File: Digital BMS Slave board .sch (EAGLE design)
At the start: 268 parts, among them J1 S7B-PH-K, J10 S3B-PH-K, J11 S4B-PH-K, J2 S4B-PH-K, J3 S4B-PH-K, J4 S6B-PH-K, J5 S2B-PH-K, J6 S2B-PH-K, J7 S2B-PH-K, J8 S2B-PH-K, J9 S3B-PH-K, Q1 BSS123, Q2 BSS123, Q3 BSS123, Q4 BSS123, Q5 BSS123, Q6 BSS123, U1 BQ79606A-Q1-HTQFP(PHP)|48, X2 PESD2CAN, X3 PESD2CAN, X4 PESD2CAN, X5 PESD2CAN

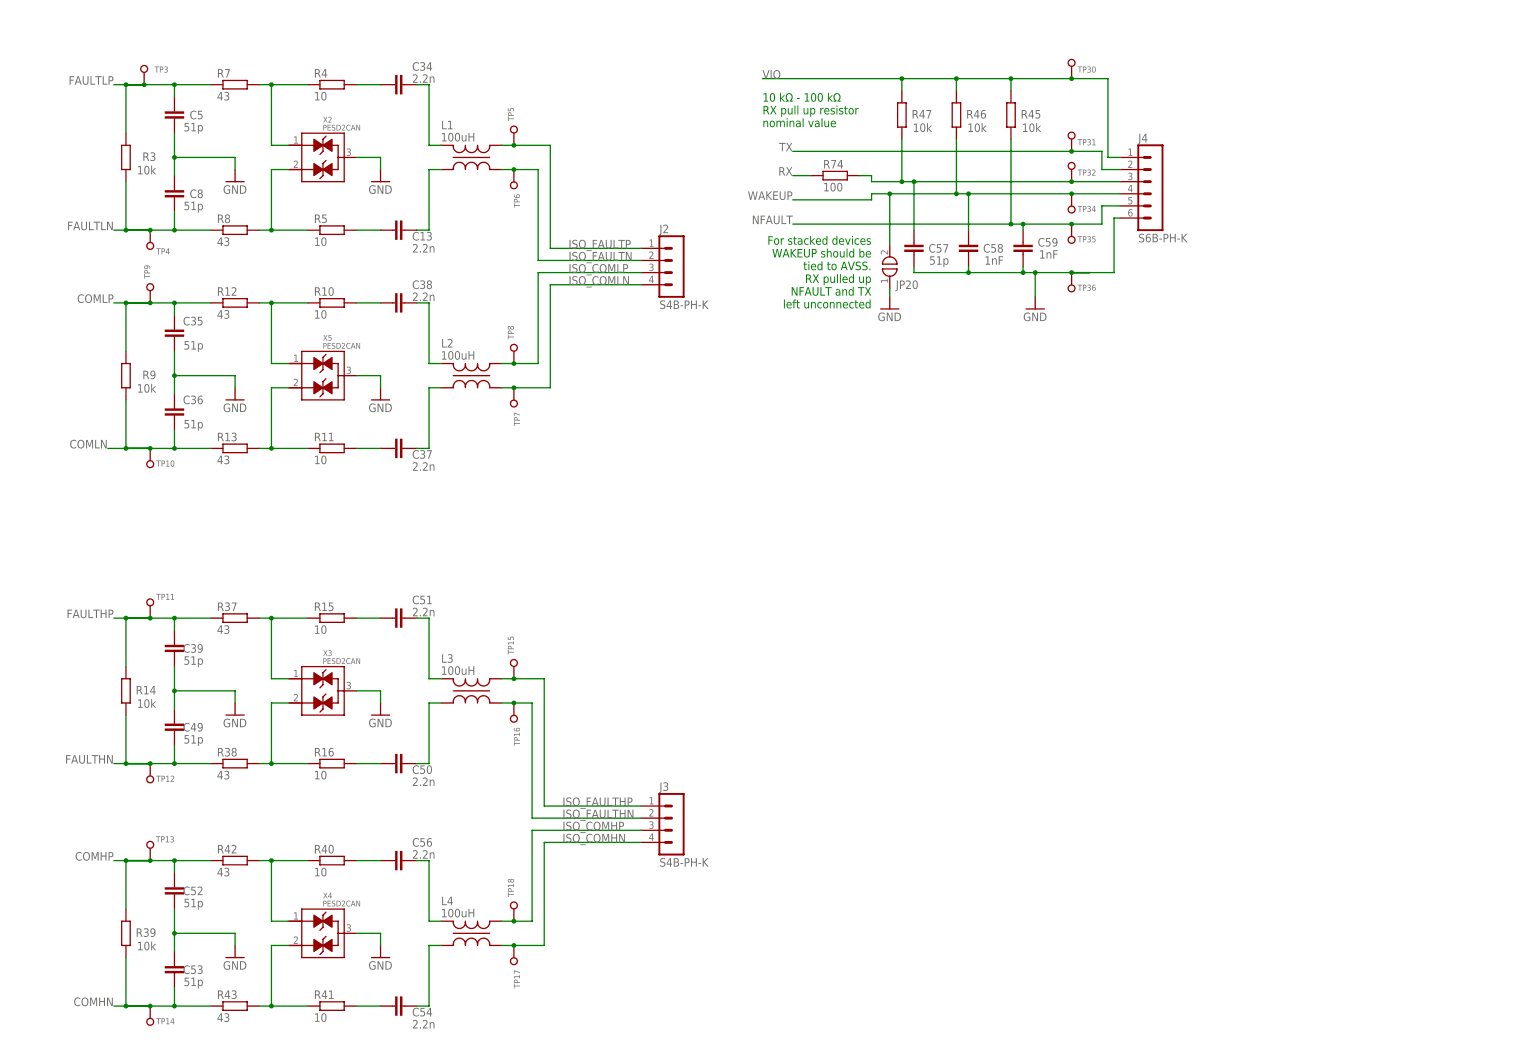
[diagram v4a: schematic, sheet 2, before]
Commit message: components placed on board
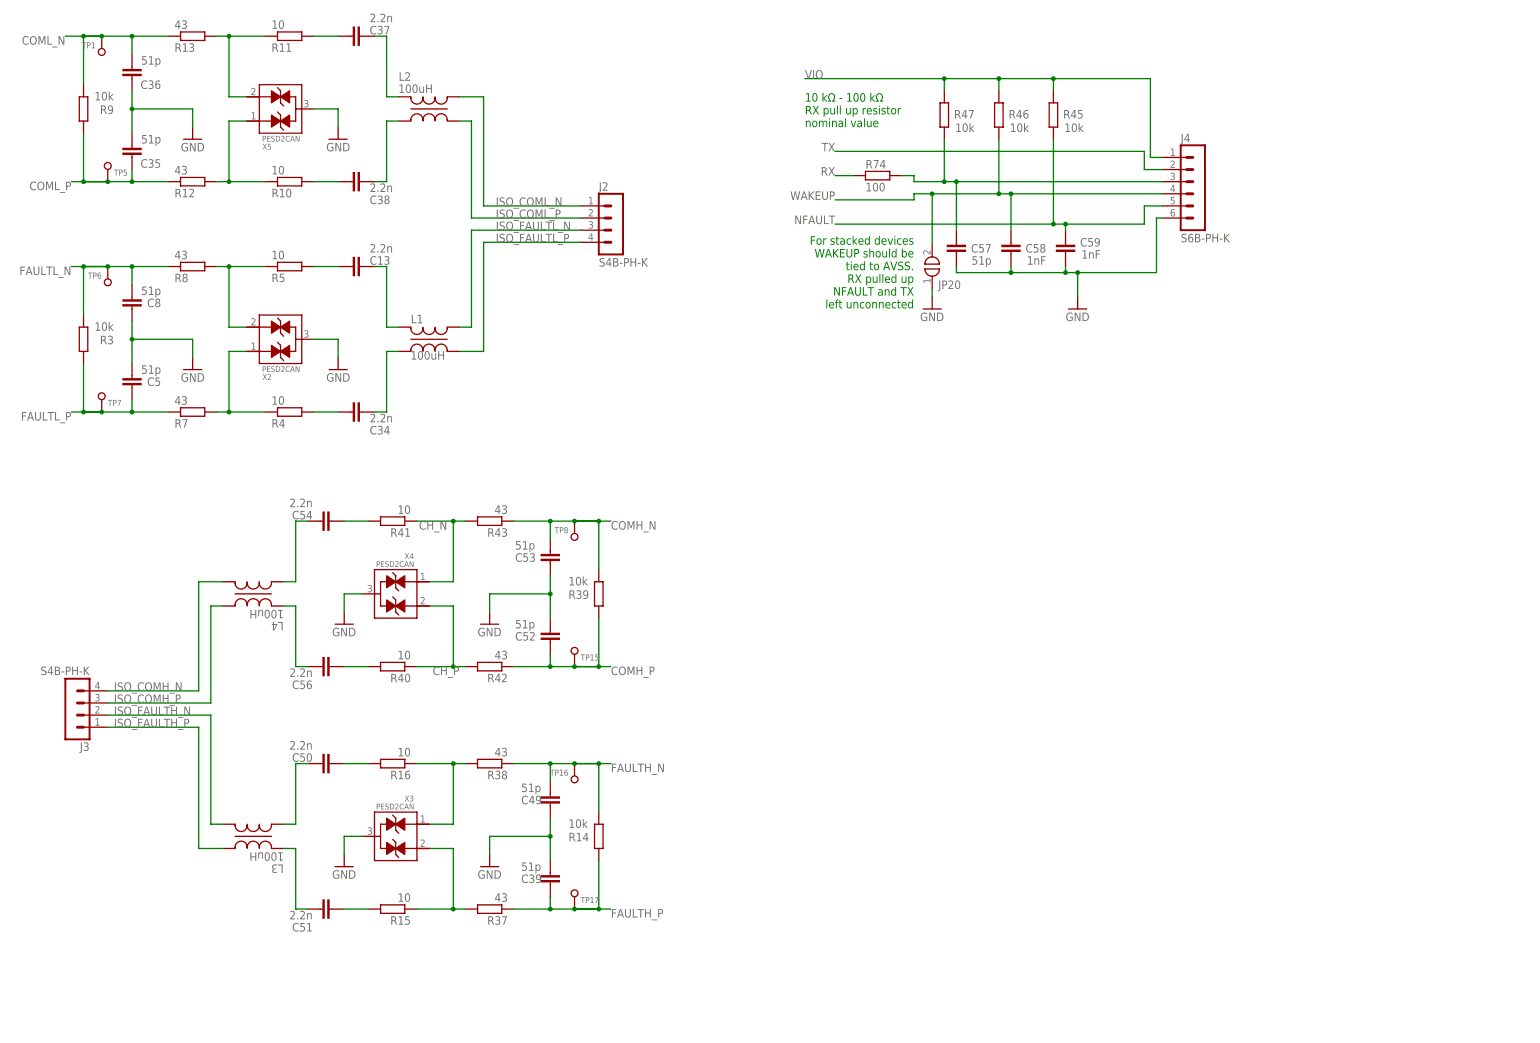
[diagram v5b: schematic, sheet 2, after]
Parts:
- removed JP4: 1x7, commonly used connectors:PINHD-1X7-OCT
- removed JP5: 2x7, pinhead:PINHD-2X7
- removed TP14, TP18, TP19, TP20, TP21, TP22, TP23, TP24, TP25, TP26, TP27, TP28, TP29, TP33: TEST_PAD2, testing:TEST_PAD2
- removed TP30, TP31, TP32, TP34, TP35, TP36, TP37, TP39, TP41, TP44, TP45, TP46, TP47, TP48, TP49, TP50: TEST_PAD, testing:TEST_PAD
- added J12: S4B-PH-K, con-jst-ph:S4B-PH-K
- J1: value S7B-PH-K -> S4B-PH-K; device con-jst-ph:S7B-PH-K -> con-jst-ph:S4B-PH-K
- TP1, TP10, TP11, TP12, TP15, TP16, TP17, TP3, TP4, TP5, TP6, TP7, TP8, TP9: value TEST_PAD2 -> TEST_PAD; device testing:TEST_PAD2 -> testing:TEST_PAD
- TP13: value TEST_PAD2 -> TEST_PAD1; device testing:TEST_PAD2 -> testing:TEST_PAD1
- U1: value BQ79606A-Q1-HTQFP(PHP)|48 -> BQ79606A-Q1-[HTQFP(PHP)|48]; device texas Instrumets:BQ79606A-Q1-HTQFP(PHP)|48 -> texas Instrumets:BQ79606A-Q1-[HTQFP(PHP)|48]
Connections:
- net 123 renamed SB1
- net 1234 renamed SB0
- net BAT105 renamed SB4
- net BAT59 renamed SB5
- net BAT65 renamed SB3
- net BAT75 renamed SB2
- net N$1 renamed BAT
- net N$2 renamed LDOIN
- net N$29 renamed EB4
- net N$32 renamed EB5
- net N$35 renamed CL1_N
- net N$36 renamed CL1_P
- net N$37 renamed FL1_N
- net N$38 renamed FL1_P
- net N$4 renamed EB6
- net N$41 renamed FL_N
- net N$42 renamed FL_P
- net N$43 renamed CL_N
- net N$44 renamed CL_P
- net N$47 renamed FH1_N
- net N$48 renamed FH1_P
- net N$5 renamed DVDD
- net N$51 renamed FH2_P
- net N$52 renamed FH2_N
- net N$53 renamed CH1_N
- net N$54 renamed CH1_P
- net N$57 renamed CH2_P
- net N$58 renamed CH2_N
- net N$64 renamed EB3
- net N$67 renamed EB2
- net N$7 renamed VPROG
- net N$72 renamed EB1
- net N$75 renamed EB0
- net N$83 renamed VC1
- net VCC15 renamed SB6
- removed net COMHN: C53.2, R39.1, R43.1, TP14.P$1, U1.COMHN
- removed net COMHP: C52.2, R39.2, R42.1, TP13.P$1, U1.COMHP
- removed net COMLN: C36.2, R13.1, R9.1, TP10.P$1, U1.COMLN
- removed net COMLP: C35.2, R12.1, R9.2, TP9.P$1, U1.COMLP
- removed net FAULTHN: C49.2, R14.1, R38.1, TP12.P$1, U1.FAULTHN
- removed net FAULTHP: C39.2, R14.2, R37.1, TP11.P$1, U1.FAULTHP
- removed net FAULTLN: C8.2, R3.1, R8.1, TP4.P$1, U1.FAULTLN
- removed net FAULTLP: C5.2, R3.2, R7.1, TP3.P$1, U1.FAULTLP
- removed net ISO_COMHN: J3.4, L4.3, TP17.P$1
- removed net ISO_COMHP: J3.3, L4.4, TP18.P$1
- removed net ISO_COMLN: J2.4, L2.3, TP7.P$1
- removed net ISO_COMLP: J2.3, L2.4, TP8.P$1
- removed net ISO_FAULTHN: J3.2, L3.3, TP16.P$1
- removed net ISO_FAULTHP: J3.1, L3.4, TP15.P$1
- removed net ISO_FAULTN: J2.2, L1.3, TP6.P$1
- removed net ISO_FAULTP: J2.1, L1.4, TP5.P$1
- removed net N$13: C26.1, C27.2, C28.2, R24.2, TP24.P$1, U1.VC5
- removed net N$14: C41.1, C42.2, C43.2, JP5.4, R31.2
- removed net N$15: C29.1, C30.2, R26.2, TP22.P$1, U1.VC3
- removed net N$16: C30.1, C31.2, C32.2, R27.2, TP21.P$1, U1.VC2
- removed net N$17: C27.1, C28.1, C29.2, R25.2, TP23.P$1, U1.VC4
- removed net N$18: C33.1, C40.2, R29.2, TP20.P$1, U1.VC0
- removed net N$26: C26.2, R23.2, TP25.P$1, U1.VC6
- removed net N$33: C60.1, C62.2, JP4.2, R48.2, R49.2, TP66.P$1
- removed net N$39: C34.1, L1.1
- removed net N$40: C13.1, L1.2
- removed net N$45: C38.1, L2.1
- removed net N$46: C37.1, L2.2
- removed net N$49: R16.1, R38.2, X3.2
- removed net N$50: R15.1, R37.2, X3.1
- removed net N$55: R41.1, R43.2, X4.2
- removed net N$56: R40.1, R42.2, X4.1
- removed net N$6: C60.2, JP4.1, R100.2, TP65.P$1
- removed net N$61: C62.1, C64.2, JP4.3, R51.2, R52.2, TP67.P$1
- removed net N$65: C64.1, C66.2, JP4.4, R53.2, R54.2, TP68.P$1
- removed net N$66: C66.1, C68.2, JP4.5, R55.2, R56.2, TP69.P$1
- removed net N$69: C44.1, C45.2, JP5.8, R33.2
- removed net N$73: C68.1, C70.2, JP4.6, R57.2, R58.2, TP70.P$1
- removed net N$74: C70.1, JP4.7, R59.2, R60.2
- removed net N$77: C48.1, C55.2, JP5.14, R36.2
- removed net N$78: C41.2, JP5.2, R30.2
- removed net N$79: C46.1, C47.1, C48.2, JP5.12, R35.2
- removed net N$80: C45.1, C46.2, C47.2, JP5.10, R34.2
- removed net N$81: C42.1, C43.1, C44.2, JP5.6, R32.2
- new net 4: J12.4
- new net CH_N: R41.1, R43.2, X4.1
- new net CH_P: R40.1, R42.2, X4.2
- new net CL2_N: C37.1, L2.1
- new net CL2_P: C38.1, L2.2
- new net COMH_N: C53.2, R39.1, R43.1, TP8.P$1, U1.COMHN
- new net COMH_P: C52.2, R39.2, R42.1, TP15.P$1, U1.COMHP
- new net COML_N: C36.2, R13.1, R9.1, TP1.P$1, U1.COMLN
- new net COML_P: C35.2, R12.1, R9.2, TP5.P$1, U1.COMLP
- new net FAULTH_N: C49.2, R14.1, R38.1, TP16.P$1, U1.FAULTHN
- new net FAULTH_P: C39.2, R14.2, R37.1, TP17.P$1, U1.FAULTHP
- new net FAULTL_N: C8.2, R3.1, R8.1, TP6.P$1, U1.FAULTLN
- new net FAULTL_P: C5.2, R3.2, R7.1, TP7.P$1, U1.FAULTLP
- new net FH_N: R16.1, R38.2, X3.1
- new net FH_P: R15.1, R37.2, X3.2
- new net FL2_N: C13.1, L1.1
- new net FL2_P: C34.1, L1.2
- new net ISO_COMH_N: J3.4, L4.3
- new net ISO_COMH_P: J3.3, L4.4
- new net ISO_COML_N: J2.1, L2.4
- new net ISO_COML_P: J2.2, L2.3
- new net ISO_FAULTH_N: J3.2, L3.3
- new net ISO_FAULTH_P: J3.1, L3.4
- new net ISO_FAULTL_N: J2.3, L1.4
- new net ISO_FAULTL_P: J2.4, L1.3
- new net VC0: C33.1, C40.2, R29.2, TP3.P$1, U1.VC0
- new net VC2: C30.1, C31.2, C32.2, R27.2, TP4.P$1, U1.VC2
- new net VC3: C29.1, C30.2, R26.2, TP9.P$1, U1.VC3
- new net VC4: C27.1, C28.1, C29.2, R25.2, TP10.P$1, U1.VC4
- new net VC5: C26.1, C27.2, C28.2, R24.2, TP11.P$1, U1.VC5
- new net VC6: C26.2, R23.2, TP12.P$1, U1.VC6
- net BAT1: now also J12.3; no longer J1.2, TP1.P$1
- net BAT2: now also J1.2; no longer J1.3, TP19.P$1
- net BAT3: now also J12.2; no longer J1.4, TP26.P$1
- net BAT4: now also J1.3; no longer J1.5, TP27.P$1
- net BAT5: now also J12.1; no longer J1.6, TP28.P$1
- net CB0: now also C48.1, C55.2, C70.1, R36.2, R59.2, R60.2, TP13.P$1; no longer JP5.13
- net CB1: now also C46.1, C47.1, C48.2, C68.1, C70.2, R35.2, R57.2, R58.2, TP70.P$1; no longer JP5.11
- net CB2: now also C45.1, C46.2, C47.2, C66.1, C68.2, R34.2, R55.2, R56.2, TP69.P$1; no longer JP5.9
- net CB3: now also C44.1, C45.2, C64.1, C66.2, R33.2, R53.2, R54.2, TP68.P$1; no longer JP5.7
- net CB4: now also C42.1, C43.1, C44.2, C62.1, C64.2, R32.2, R51.2, R52.2, TP67.P$1; no longer JP5.5
- net CB5: now also C41.1, C42.2, C43.2, C60.1, C62.2, R31.2, R48.2, R49.2, TP66.P$1; no longer JP5.3
- net CB6: now also C41.2, C60.2, R100.2, R30.2, TP65.P$1; no longer JP5.1
- net GND: no longer TP33.P$1, TP36.P$1, TP47.P$1, TP50.P$1
- net GPIO4: now also JP1.8; no longer JP1.12
- net GPIO6: now also JP1.12; no longer JP1.8
- net N$10: no longer TP37.P$1
- net N$11: no longer TP39.P$1
- net N$25: no longer TP46.P$1
- net N$27: no longer TP49.P$1
- net N$8: no longer TP41.P$1
- net N$9: no longer TP44.P$1
- net NFAULT: no longer TP35.P$1
- net RX1: no longer TP32.P$1
- net TSREF: no longer TP45.P$1, TP48.P$1
- net TX: no longer TP31.P$1
- net VCC: now also J1.4; no longer J1.7, TP29.P$1
- net VIO: no longer TP30.P$1
- net WAKEUP: no longer TP34.P$1
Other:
- moved on the sheet: C13, C34, C35, C36, C37, C38, C39, C41, C42, C43, C44, C45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

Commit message: Go home
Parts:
- TP1, TP10, TP11, TP12, TP15, TP16, TP17, TP2, TP3, TP38, TP4, TP40, TP42, TP43, TP5, TP51, TP52, TP6, TP7, TP8, TP9: value TEST_PAD -> TEST_PAD-[1MM]; device testing:TEST_PAD -> testing:TEST_PAD-[1MM]
- TP13, TP53, TP54, TP55, TP56, TP57, TP58, TP59, TP60, TP61, TP62, TP63, TP64, TP65, TP66, TP67, TP68, TP69, TP70: value TEST_PAD1 -> TEST_PAD-[1.27MM]; device testing:TEST_PAD1 -> testing:TEST_PAD-[1.27MM]

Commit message: COM and IC CAP routed
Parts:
- added JP4: (no value), pinhead:PINHD-1X2
- U1: value BQ79606A-Q1-[HTQFP(PHP)|48] -> BQ79606A-Q1-HTQFP|48|9VIA; device texas Instrumets:BQ79606A-Q1-[HTQFP(PHP)|48] -> texas Instrumets:BQ79606A-Q1-HTQFP|48|9VIA
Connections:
- new net N$2: JP4.2, R6.2
- net BAT1: now also JP6.12; no longer JP6.11
- net BAT2: now also JP6.10; no longer JP6.9
- net BAT3: now also JP6.8; no longer JP6.7
- net BAT4: now also JP6.6; no longer JP6.5
- net BAT5: now also JP6.4; no longer JP6.3
- net GND: now also JP6.14, U1.PAD; no longer JP6.13
- net SB0: now also JP6.13; no longer JP6.14
- net SB1: now also JP6.11; no longer JP6.12
- net SB2: now also JP6.9; no longer JP6.10
- net SB3: now also JP6.7; no longer JP6.8
- net SB4: now also JP6.5; no longer JP6.6
- net SB5: now also JP6.3; no longer JP6.4
- net SB6: now also JP6.1; no longer JP6.2
- net VCC: now also JP6.2; no longer JP6.1
- net VPROG: now also JP4.1; no longer R6.2
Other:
- moved on the sheet: C12, R6, U1

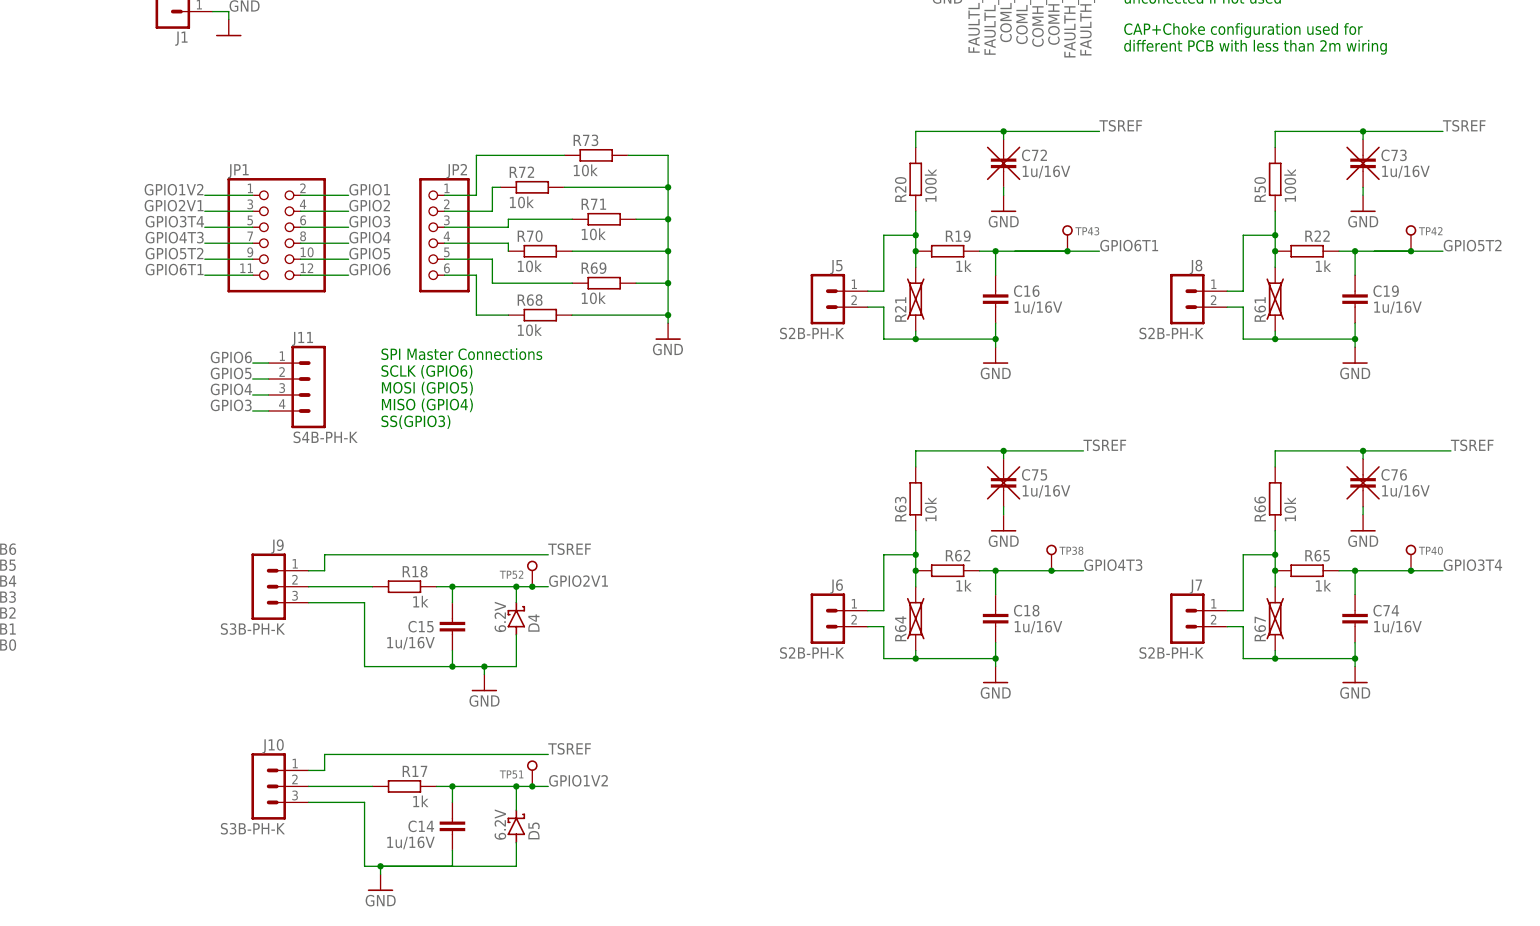
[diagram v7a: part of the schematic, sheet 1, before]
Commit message: GPIO routed
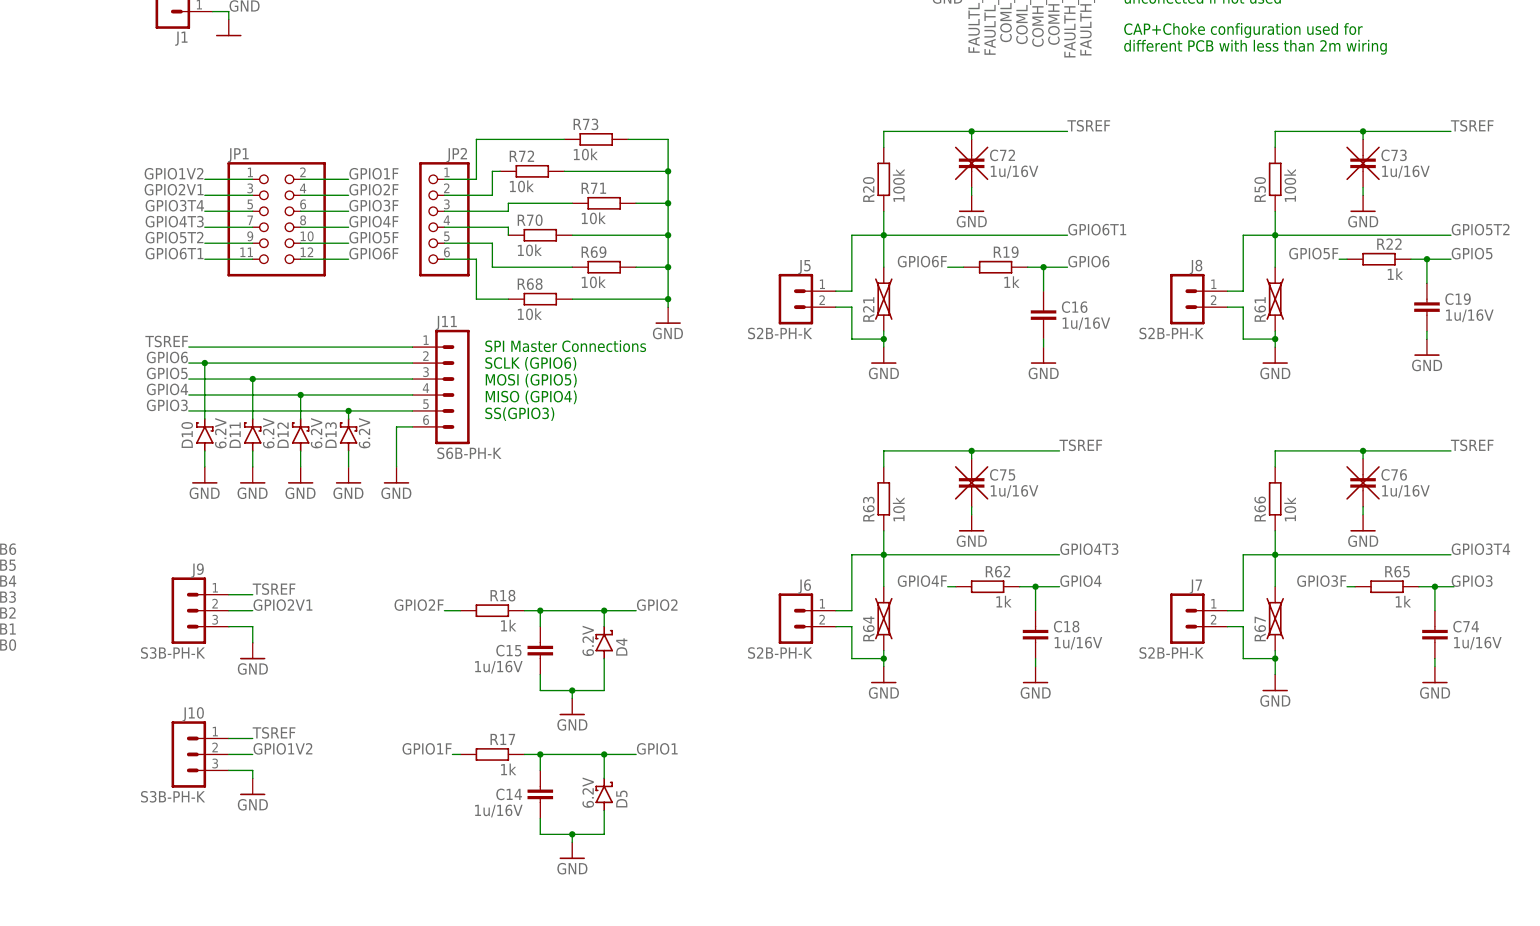
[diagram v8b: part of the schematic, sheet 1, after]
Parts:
- removed TP38, TP40, TP42, TP43, TP51, TP52: TEST_PAD-[1MM], testing:TEST_PAD-[1MM]
- added D10, D11, D12, D13: 6.2V, Semiconductor_devices:SOD323-ZENER
- J11: value S4B-PH-K -> S6B-PH-K; device con-jst-ph:S4B-PH-K -> con-jst-ph:S6B-PH-K
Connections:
- removed net N$10: J6.1, R62.2, R63.1, R64.2
- removed net N$11: J7.1, R65.2, R66.1, R67.2
- removed net N$25: J10.2, R17.2
- removed net N$27: J9.2, R18.2
- removed net N$8: J8.1, R22.2, R50.1, R61.2
- removed net N$9: J5.1, R19.2, R20.1, R21.2
- new net GPIO1F: JP1.2, R17.2
- new net GPIO2F: JP1.4, R18.2
- new net GPIO3F: JP1.6, R65.2
- new net GPIO4F: JP1.8, R62.2
- new net GPIO5F: JP1.10, R22.2
- new net GPIO6F: JP1.12, R19.2
- net GND: now also D10.A, D11.A, D12.A, D13.A, J11.6
- net GPIO1: now also C14.2, D5.C, R17.1; no longer JP1.2
- net GPIO1V2: now also J10.2; no longer C14.2, D5.C, R17.1, TP51.P$1
- net GPIO2: now also C15.2, D4.C, R18.1; no longer JP1.4
- net GPIO2V1: now also J9.2; no longer C15.2, D4.C, R18.1, TP52.P$1
- net GPIO3: now also C74.2, D13.C, J11.5, R65.1; no longer J11.4, JP1.6
- net GPIO3T4: now also J7.1, R66.1, R67.2; no longer C74.2, R65.1, TP40.P$1
- net GPIO4: now also C18.2, D12.C, J11.4, R62.1; no longer J11.3, JP1.8
- net GPIO4T3: now also J6.1, R63.1, R64.2; no longer C18.2, R62.1, TP38.P$1
- net GPIO5: now also C19.2, D11.C, J11.3, R22.1; no longer J11.2, JP1.10
- net GPIO5T2: now also J8.1, R50.1, R61.2; no longer C19.2, R22.1, TP42.P$1
- net GPIO6: now also C16.2, D10.C, J11.2, R19.1; no longer J11.1, JP1.12
- net GPIO6T1: now also J5.1, R20.1, R21.2; no longer C16.2, R19.1, TP43.P$1
- net TSREF: now also J11.1
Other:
- moved on the sheet: C14, C15, C16, C18, C19, C72, C74, C75, D4, D5, J10, J5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
